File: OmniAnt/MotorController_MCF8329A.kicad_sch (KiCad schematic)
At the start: 25 parts, among them J10 Conn_01x01, J12 Conn_01x01, J8 Conn_01x01, Q1 NTMFS4C324NT1G, Q2 NTMFS4C324NT1G, Q3 NTMFS4C324NT1G, Q4 NTMFS4C324NT1G, Q5 NTMFS4C324NT1G, Q6 NTMFS4C324NT1G, U4 MCF8329A1IREER

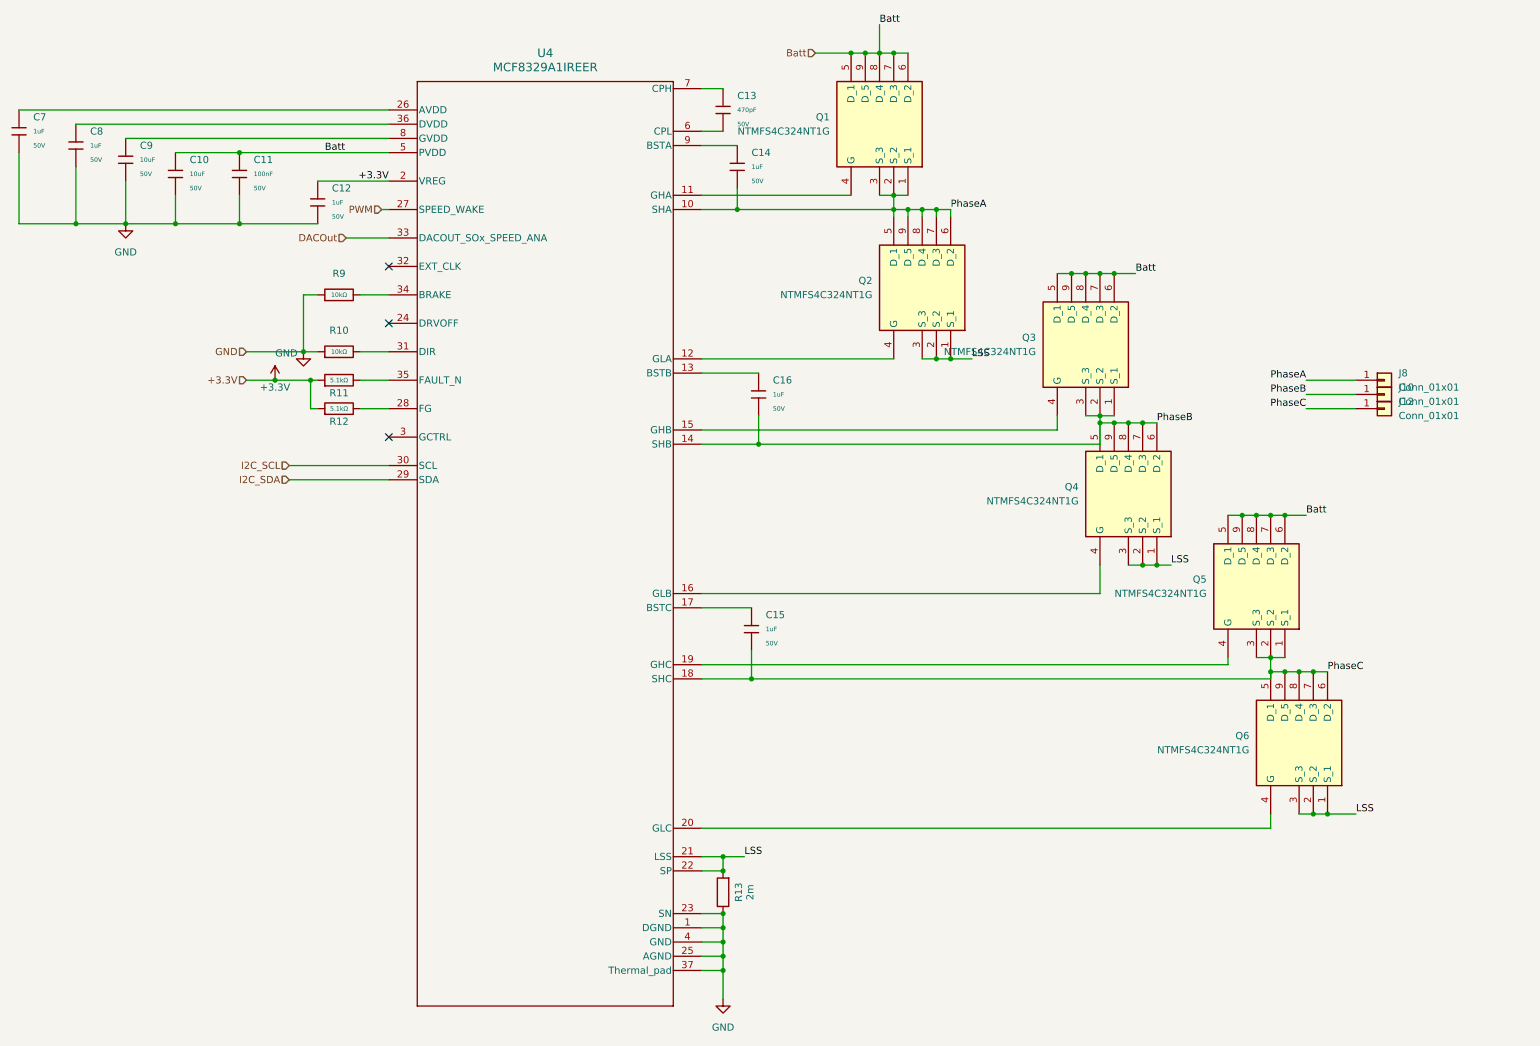
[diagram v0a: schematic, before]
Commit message: Major progress on the motor driver layout. Lots of learning with how to draw traces and pours.
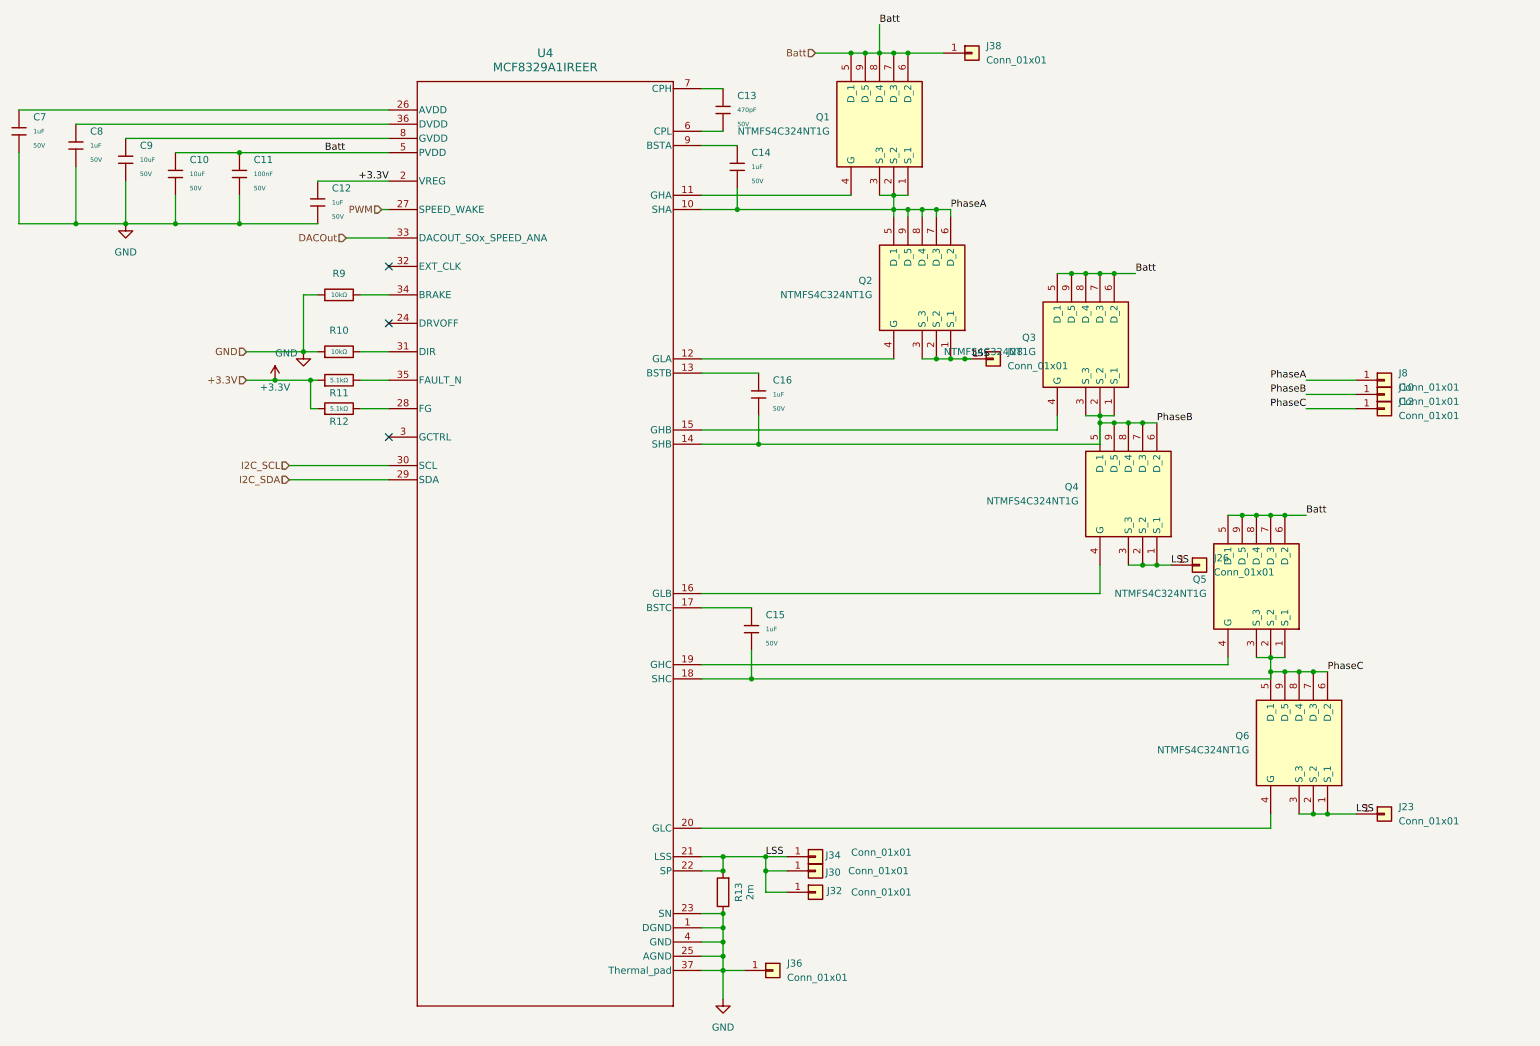
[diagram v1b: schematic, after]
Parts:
- added J23, J26, J28, J30, J32, J34: Conn_01x01, Connector_Wire:SolderWire-0.25sqmm_1x01_D0.65mm_OD1.7mm, symbol Connector_Generic:Conn_01x01
- added J36, J38: Conn_01x01, SolderWire-1.5sqmm_1x01_D1.7mm_OD3mm, symbol Connector_Generic:Conn_01x01
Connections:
- net Batt: now also J38.1 (Pin_1)
- net GND: now also J36.1 (Pin_1)
- net LSS: now also J23.1 (Pin_1), J26.1 (Pin_1), J28.1 (Pin_1), J30.1 (Pin_1), J32.1 (Pin_1), J34.1 (Pin_1)

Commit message: I made more progress on the layout. I'm working on adding the extra protection components to the driver circuit.
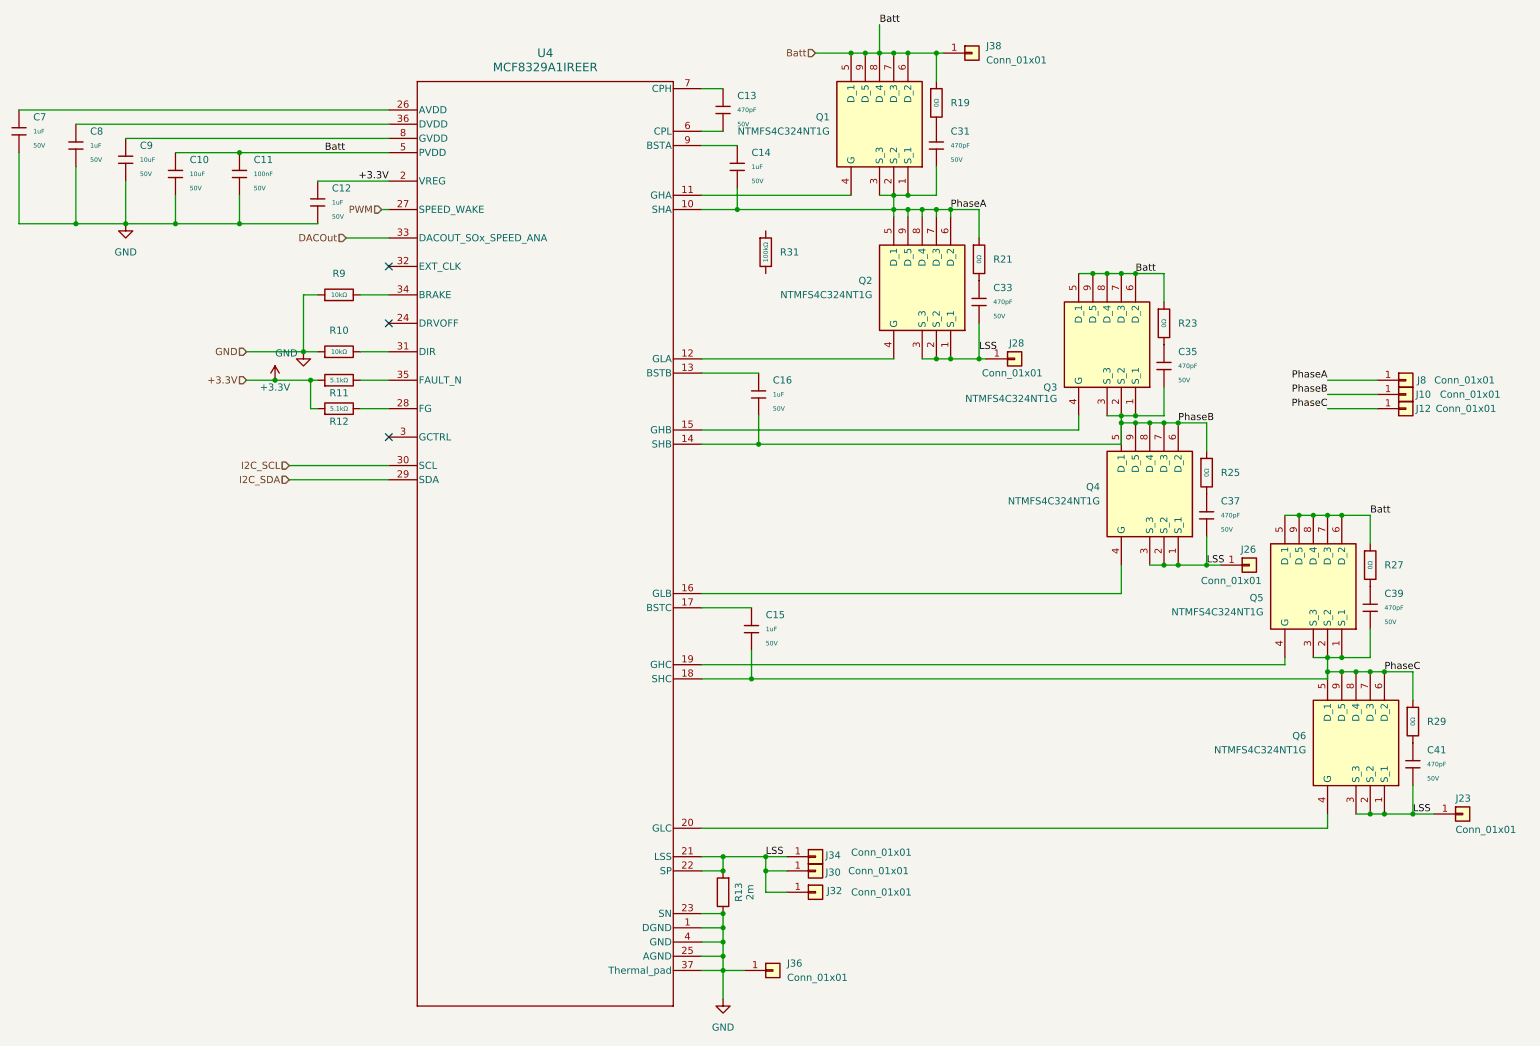
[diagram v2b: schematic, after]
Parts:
- added C31, C33, C35, C37, C39, C41: 470pF, PCM_JLCPCB:C_0603, symbol PCM_JLCPCB-Capacitors:0603,470pF
- added R19, R21, R23, R25, R27, R29: 0Ω, PCM_JLCPCB:R_0402, symbol PCM_JLCPCB-Resistors:0402,0Ω
- added R31: 100kΩ, PCM_JLCPCB:R_0402, symbol PCM_JLCPCB-Resistors:0402,100kΩ
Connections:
- net Batt: now also R19.1, R23.1, R27.1
- net LSS: now also C33.2, C37.2, C41.2
- net PhaseA: now also C31.2, R21.1
- net PhaseB: now also C35.2, R25.1
- net PhaseC: now also C39.2, R29.1
- new net: C39.1, R27.2
- new net: C31.1, R19.2
- new net: C41.1, R29.2
- new net: C33.1, R21.2
- new net: C37.1, R25.2
- new net: C35.1, R23.2
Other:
- moved on the sheet: J10, J12, J23, J26, J28, J8, Q3, Q4, Q5, Q6

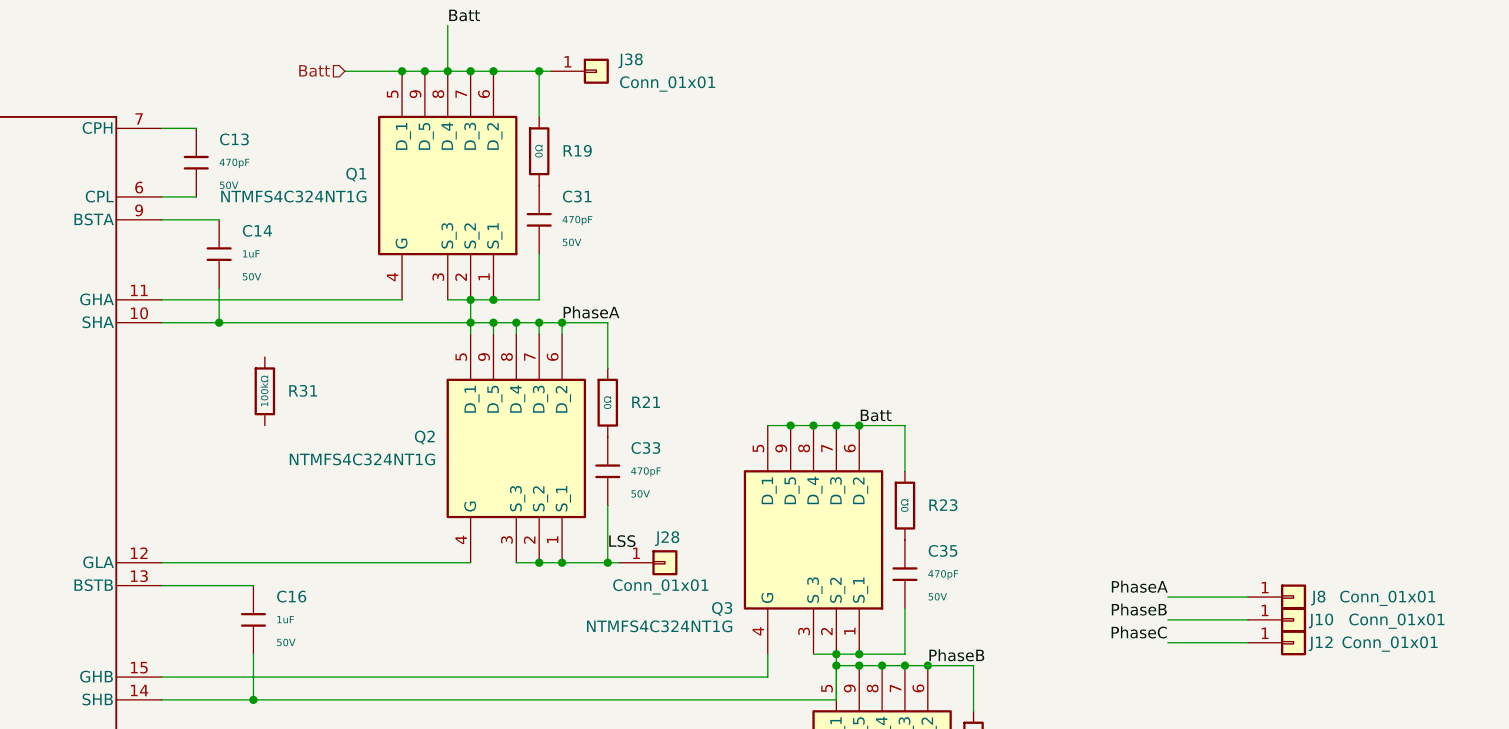
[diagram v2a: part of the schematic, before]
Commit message: Ok I did a lot of reading today. I'm going to split each FET into a sheet, so I can add the external circuitry more easily.
I may need to source a different FET. The one I selected has a good EAS, but the rating is only for 11A. and Ideally I would be able to do 19 or 20A. I'm sure I will never do that much current , but relying on the mosfet to handle things seems better than adding an additional tvs diode. Snubber is the way to go for sure to keep things cool.
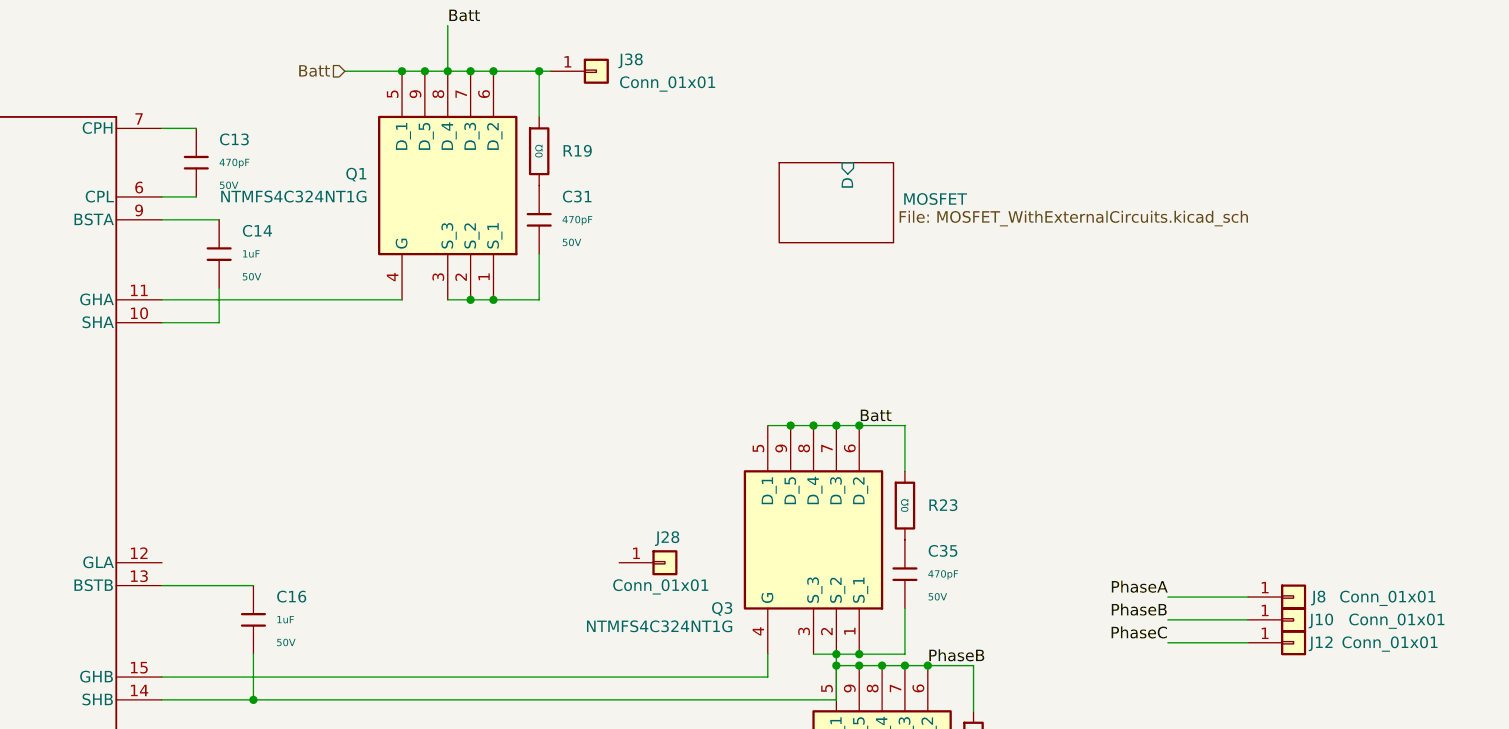
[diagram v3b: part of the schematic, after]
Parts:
- removed C33: 470pF, PCM_JLCPCB:C_0603, symbol PCM_JLCPCB-Capacitors:0603,470pF
- removed Q2: NTMFS4C324NT1G, Footprints:NVMFS5C442NLWFAFT1G, symbol NTMFS4C324NT1G:NTMFS4C324NT1G
- removed R21: 0Ω, PCM_JLCPCB:R_0402, symbol PCM_JLCPCB-Resistors:0402,0Ω
- removed R31: 100kΩ, PCM_JLCPCB:R_0402, symbol PCM_JLCPCB-Resistors:0402,100kΩ
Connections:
- net LSS: no longer J28.1 (Pin_1)
- net PhaseA: no longer C14.2, C31.2, Q1.1 (S_1), Q1.2 (S_2), Q1.3 (S_3), U4.10 (SHA)
- new net: C31.2, Q1.1 (S_1), Q1.2 (S_2), Q1.3 (S_3)
- new net: C14.2, U4.10 (SHA)
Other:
- added sheet MOSFET (MOSFET_WithExternalCircuits.kicad_sch)
